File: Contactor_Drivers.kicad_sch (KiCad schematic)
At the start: 37 parts, among them Con1 LED, Con2 LED, Con3 LED, Con4 LED, J4 Conn_01x05, J5 Conn_01x04, J6 Conn_01x04, J7 Conn_01x04, J8 Conn_01x04, Q4 IRLML0030, Q5 IRLML0030, Q6 IRLML0030, Q7 IRLML0030

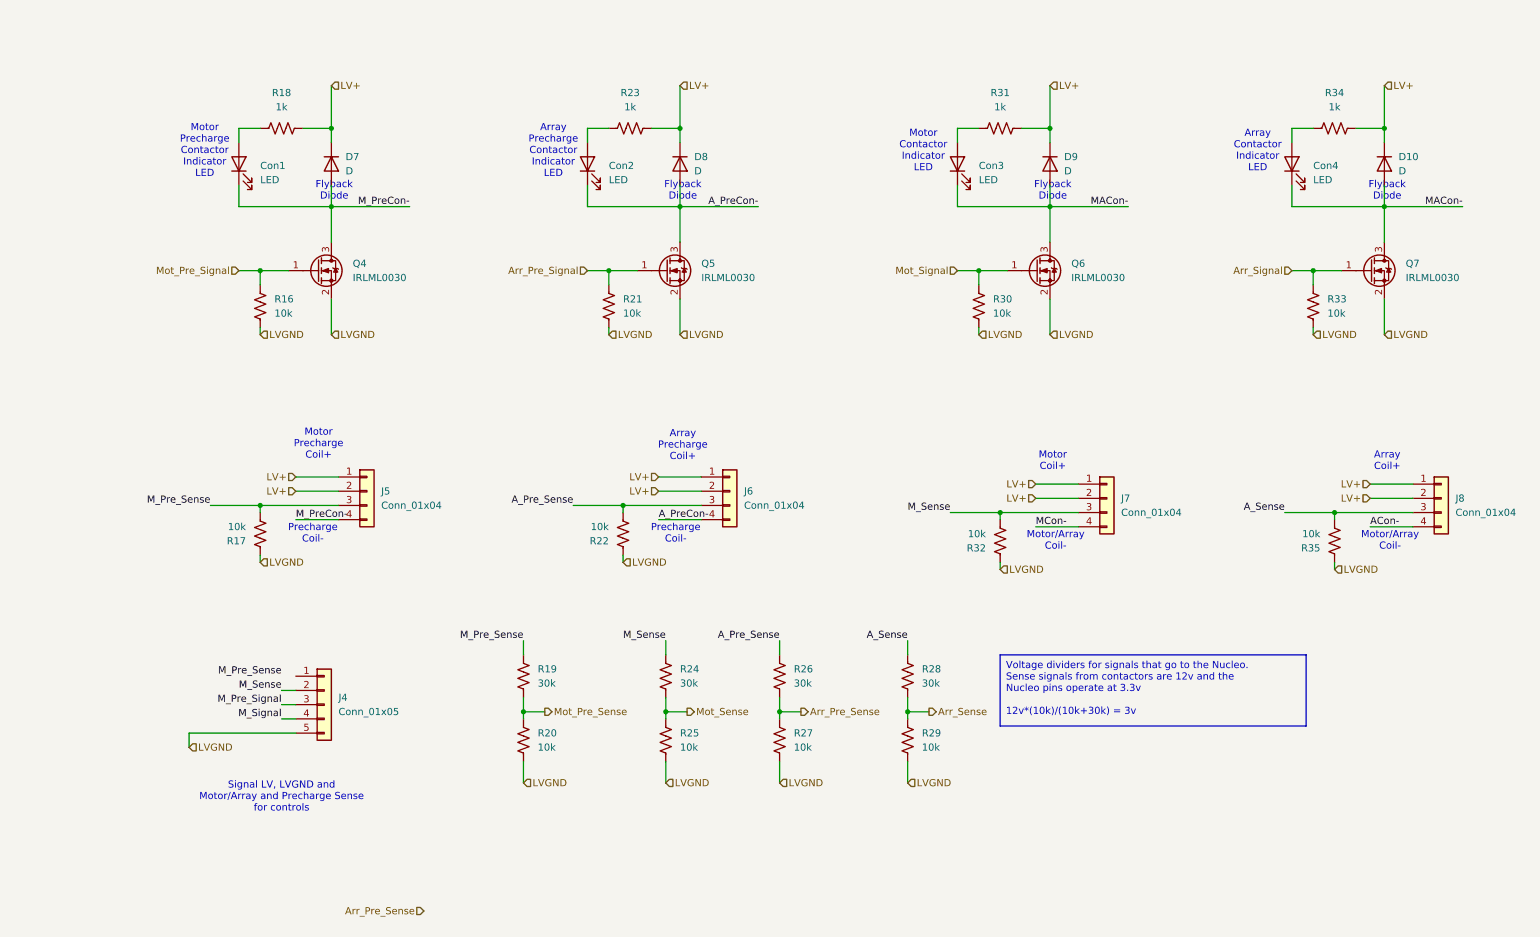
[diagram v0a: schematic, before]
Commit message: fixed some ERC errors, incorrect connectors
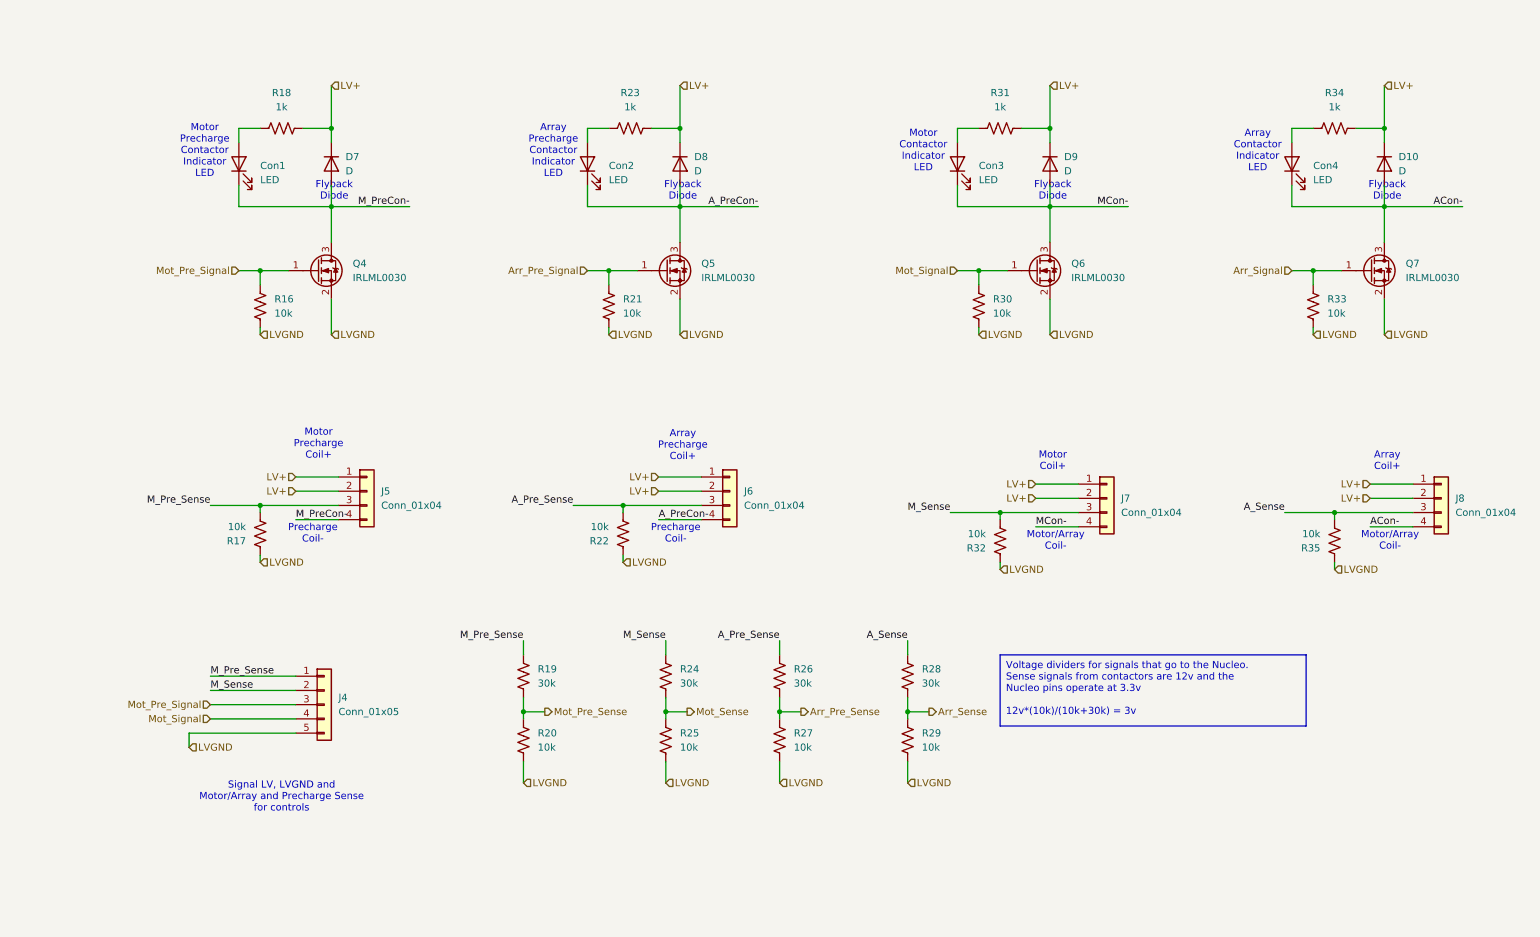
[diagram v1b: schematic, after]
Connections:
- net M_Pre_Signal is gone; now on net Mot_Pre_Signal: J4.3 (Pin_3)
- net M_Signal is gone; now on net Mot_Signal: J4.4 (Pin_4)
- net ACon-: now also Con4.1 (K), D10.2 (A), Q7.3 (D)
- net MCon-: now also Con3.1 (K), D9.2 (A), Q6.3 (D)
- net M_Pre_Sense: now also J4.1 (Pin_1)
- removed net MACon-: Con3.1 (K), Con4.1 (K), D10.2 (A), D9.2 (A), Q6.3 (D), Q7.3 (D)
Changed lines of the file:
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@@
 	(wire
 		(pts
-			(xy 58.42 148.59) (xy 60.96 148.59)
+			(xy 45.72 148.59) (xy 60.96 148.59)
 		)
 		(stroke
@@
 	(wire
 		(pts
+			(xy 45.72 140.97) (xy 60.96 140.97)
+		)
+		(stroke
+			(width 0)
+			(type default)
+		)
+	)
+	(wire
+		(pts
 			(xy 54.61 110.49) (xy 54.61 111.76)
 		)
@@
 	(wire
 		(pts
-			(xy 58.42 146.05) (xy 60.96 146.05)
+			(xy 45.72 146.05) (xy 60.96 146.05)
 		)
 		(stroke
@@
 	(wire
 		(pts
-			(xy 58.42 143.51) (xy 60.96 143.51)
+			(xy 45.72 143.51) (xy 60.96 143.51)
 		)
 		(stroke
@@
 		)
 	)
-	(label "MACon-"
+	(label "ACon-"
 		(at 269.24 57.15 180)
-		(fields_autoplaced yes)
-		(effects
-			(font
-				(size 1.27 1.27)
-			)
-			(justify right bottom)
-		)
-	)
-	(label "M_Pre_Signal"
-		(at 58.42 146.05 180)
 		(fields_autoplaced yes)
 		(effects
@@
 		)
 	)
-	(label "M_Signal"
-		(at 58.42 148.59 180)
-		(fields_autoplaced yes)
-		(effects
-			(font
-				(size 1.27 1.27)
-			)
-			(justify right bottom)
-		)
-	)
 	(label "ACon-"
 		(at 252.73 114.3 0)
@@
 		)
 	)
-	(label "MACon-"
+	(label "MCon-"
 		(at 209.55 57.15 180)
 		(fields_autoplaced yes)
@@
 	)
 	(label "M_Pre_Sense"
-		(at 58.42 140.97 180)
-		(fields_autoplaced yes)
-		(effects
-			(font
-				(size 1.27 1.27)
-			)
-			(justify right bottom)
+		(at 45.72 140.97 0)
+		(fields_autoplaced yes)
+		(effects
+			(font
+				(size 1.27 1.27)
+			)
+			(justify left bottom)
 		)
 	)
@@
 	)
 	(label "M_Sense"
-		(at 58.42 143.51 180)
-		(fields_autoplaced yes)
-		(effects
-			(font
-				(size 1.27 1.27)
-			)
-			(justify right bottom)
+		(at 45.72 143.51 0)
+		(fields_autoplaced yes)
+		(effects
+			(font
+				(size 1.27 1.27)
+			)
+			(justify left bottom)
 		)
 	)
@@
 		)
 	)
+	(hierarchical_label "Mot_Pre_Signal"
+		(shape input)
+		(at 45.72 146.05 180)
+		(fields_autoplaced yes)
+		(effects
+			(font
+				(size 1.27 1.27)
+			)
+			(justify right)
+		)
+	)
 	(hierarchical_label "Arr_Pre_Signal"
 		(shape input)
@@
 			)
 			(justify left)
-		)
-	)
-	(hierarchical_label "Arr_Pre_Sense"
-		(shape input)
-		(at 83.82 182.88 180)
-		(fields_autoplaced yes)
-		(effects
-			(font
-				(size 1.27 1.27)
-			)
-			(justify right)
 		)
 	)
@@
 		)
 	)
+	(hierarchical_label "Mot_Signal"
+		(shape input)
+		(at 45.72 148.59 180)
+		(fields_autoplaced yes)
+		(effects
+			(font
+				(size 1.27 1.27)
+			)
+			(justify right)
+		)
+	)

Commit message: started on HV layout
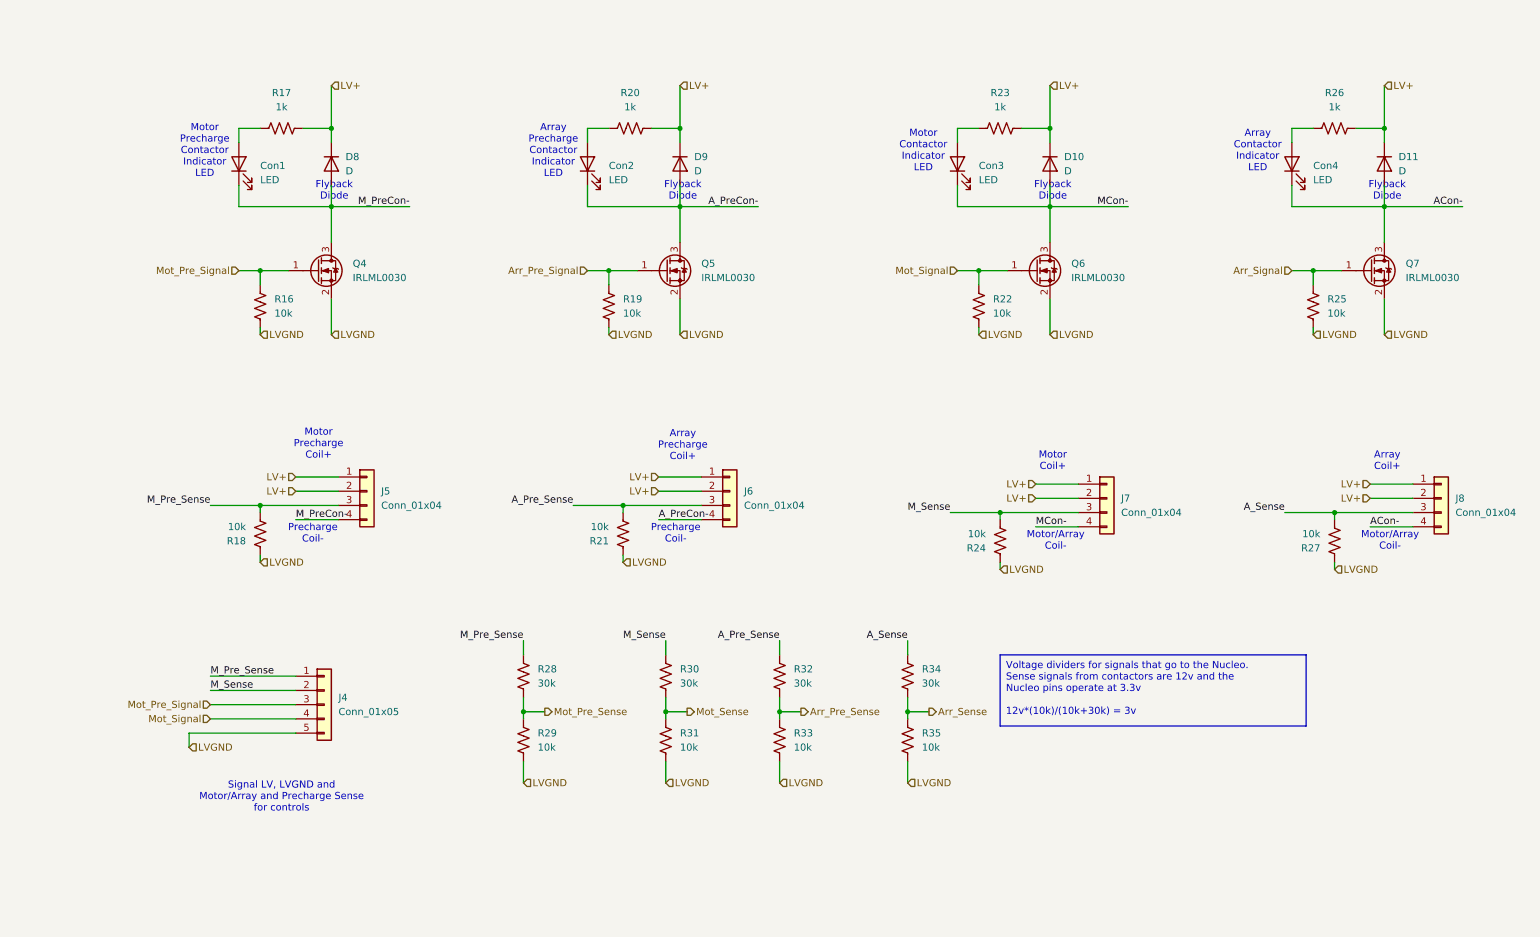
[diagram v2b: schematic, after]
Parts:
- renumbered D9 to D10, D10 to D11, D7 to D8, D8 to D9, R18 to R17, R17 to R18, R21 to R19, R23 to R20, R22 to R21, R30 to R22, R31 to R23, R32 to R24, R33 to R25, R34 to R26, R35 to R27, R19 to R28, R20 to R29, R24 to R30, R25 to R31, R26 to R32, R27 to R33, R28 to R34, R29 to R35
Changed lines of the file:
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@@
 		(on_board yes)
 		(dnp no)
-		(property "Reference" "R22"
+		(property "Reference" "R21"
 			(at 116.84 116.8401 0)
 			(effects
@@
 			(project "ActivePrecharge"
 				(path "/b9847a31-2b3b-47ca-9561-fab506416f6d/c0036b4f-8078-47a1-85ab-72dbdcf28d35"
-					(reference "R22")
+					(reference "R21")
 					(unit 1)
 				)
@@
 		(dnp no)
 		(fields_autoplaced yes)
-		(property "Reference" "R19"
+		(property "Reference" "R28"
 			(at 104.14 139.6999 0)
 			(effects
@@
 			(project "ActivePrecharge"
 				(path "/b9847a31-2b3b-47ca-9561-fab506416f6d/c0036b4f-8078-47a1-85ab-72dbdcf28d35"
-					(reference "R19")
+					(reference "R28")
 					(unit 1)
 				)
@@
 		(on_board yes)
 		(dnp no)
-		(property "Reference" "R30"
+		(property "Reference" "R22"
 			(at 185.42 73.6599 0)
 			(effects
@@
 			(project "ActivePrecharge"
 				(path "/b9847a31-2b3b-47ca-9561-fab506416f6d/c0036b4f-8078-47a1-85ab-72dbdcf28d35"
-					(reference "R30")
+					(reference "R22")
 					(unit 1)
 				)
@@
 		(dnp no)
 		(fields_autoplaced yes)
-		(property "Reference" "D10"
+		(property "Reference" "D11"
 			(at 257.81 48.2599 90)
 			(effects
@@
 			(project "ActivePrecharge"
 				(path "/b9847a31-2b3b-47ca-9561-fab506416f6d/c0036b4f-8078-47a1-85ab-72dbdcf28d35"
-					(reference "D10")
+					(reference "D11")
 					(unit 1)
 				)
@@
 		(dnp no)
 		(fields_autoplaced yes)
-		(property "Reference" "R18"
+		(property "Reference" "R17"
 			(at 58.42 36.83 90)
 			(effects
@@
 			(project "ActivePrecharge"
 				(path "/b9847a31-2b3b-47ca-9561-fab506416f6d/c0036b4f-8078-47a1-85ab-72dbdcf28d35"
-					(reference "R18")
+					(reference "R17")
 					(unit 1)
 				)
@@
 		(dnp no)
 		(fields_autoplaced yes)
-		(property "Reference" "R20"
+		(property "Reference" "R29"
 			(at 104.14 151.1299 0)
 			(effects
@@
 			(project "ActivePrecharge"
 				(path "/b9847a31-2b3b-47ca-9561-fab506416f6d/c0036b4f-8078-47a1-85ab-72dbdcf28d35"
-					(reference "R20")
+					(reference "R29")
 					(unit 1)
 				)
@@
 		(dnp no)
 		(fields_autoplaced yes)
-		(property "Reference" "D8"
+		(property "Reference" "D9"
 			(at 132.08 48.2599 90)
 			(effects
@@
 			(project "ActivePrecharge"
 				(path "/b9847a31-2b3b-47ca-9561-fab506416f6d/c0036b4f-8078-47a1-85ab-72dbdcf28d35"
-					(reference "D8")
+					(reference "D9")
 					(unit 1)
 				)
@@
 		(dnp no)
 		(fields_autoplaced yes)
-		(property "Reference" "R28"
+		(property "Reference" "R34"
 			(at 172.72 139.6999 0)
 			(effects
@@
 			(project "ActivePrecharge"
 				(path "/b9847a31-2b3b-47ca-9561-fab506416f6d/c0036b4f-8078-47a1-85ab-72dbdcf28d35"
-					(reference "R28")
+					(reference "R34")
 					(unit 1)
 				)
@@
 		(dnp no)
 		(fields_autoplaced yes)
-		(property "Reference" "R25"
+		(property "Reference" "R31"
 			(at 129.54 151.1299 0)
 			(effects
@@
 			(project "ActivePrecharge"
 				(path "/b9847a31-2b3b-47ca-9561-fab506416f6d/c0036b4f-8078-47a1-85ab-72dbdcf28d35"
-					(reference "R25")
+					(reference "R31")
 					(unit 1)
 				)
@@
 		(dnp no)
 		(fields_autoplaced yes)
-		(property "Reference" "D9"
+		(property "Reference" "D10"
 			(at 198.12 48.2599 90)
 			(effects
@@
 			(project "ActivePrecharge"
 				(path "/b9847a31-2b3b-47ca-9561-fab506416f6d/c0036b4f-8078-47a1-85ab-72dbdcf28d35"
-					(reference "D9")
+					(reference "D10")
 					(unit 1)
 				)
@@
 		(dnp no)
 		(fields_autoplaced yes)
-		(property "Reference" "R24"
+		(property "Reference" "R30"
 			(at 129.54 139.6999 0)
 			(effects
@@
 			(project "ActivePrecharge"
 				(path "/b9847a31-2b3b-47ca-9561-fab506416f6d/c0036b4f-8078-47a1-85ab-72dbdcf28d35"
-					(reference "R24")
+					(reference "R30")
 					(unit 1)
 				)
@@
 		(on_board yes)
 		(dnp no)
-		(property "Reference" "R33"
+		(property "Reference" "R25"
 			(at 245.11 73.6599 0)
 			(effects
@@
 			(project "ActivePrecharge"
 				(path "/b9847a31-2b3b-47ca-9561-fab506416f6d/c0036b4f-8078-47a1-85ab-72dbdcf28d35"
-					(reference "R33")
+					(reference "R25")
 					(unit 1)
 				)
@@
 		(dnp no)
 		(fields_autoplaced yes)
-		(property "Reference" "R29"
+		(property "Reference" "R35"
 			(at 172.72 151.1299 0)
 			(effects
@@
 			(project "ActivePrecharge"
 				(path "/b9847a31-2b3b-47ca-9561-fab506416f6d/c0036b4f-8078-47a1-85ab-72dbdcf28d35"
-					(reference "R29")
+					(reference "R35")
 					(unit 1)
 				)
@@
 		(on_board yes)
 		(dnp no)
-		(property "Reference" "R21"
+		(property "Reference" "R19"
 			(at 119.38 73.6599 0)
 			(effects
@@
 			(project "ActivePrecharge"
 				(path "/b9847a31-2b3b-47ca-9561-fab506416f6d/c0036b4f-8078-47a1-85ab-72dbdcf28d35"
-					(reference "R21")
+					(reference "R19")
 					(unit 1)
 				)
@@
 		(on_board yes)
 		(dnp no)
-		(property "Reference" "R17"
+		(property "Reference" "R18"
 			(at 52.07 116.8401 0)
 			(effects
@@
 			(project "ActivePrecharge"
 				(path "/b9847a31-2b3b-47ca-9561-fab506416f6d/c0036b4f-8078-47a1-85ab-72dbdcf28d35"
-					(reference "R17")
+					(reference "R18")
 					(unit 1)
 				)
@@
 		(dnp no)
 		(fields_autoplaced yes)
-		(property "Reference" "R31"
+		(property "Reference" "R23"
 			(at 186.69 36.83 90)
 			(effects
@@
 			(project "ActivePrecharge"
 				(path "/b9847a31-2b3b-47ca-9561-fab506416f6d/c0036b4f-8078-47a1-85ab-72dbdcf28d35"
-					(reference "R31")
+					(reference "R23")
 					(unit 1)
 				)
@@
 		(dnp no)
 		(fields_autoplaced yes)
-		(property "Reference" "R26"
+		(property "Reference" "R32"
 			(at 149.86 139.6999 0)
 			(effects
@@
 			(project "ActivePrecharge"
 				(path "/b9847a31-2b3b-47ca-9561-fab506416f6d/c0036b4f-8078-47a1-85ab-72dbdcf28d35"
-					(reference "R26")
+					(reference "R32")
 					(unit 1)
 				)
@@
 		(dnp no)
 		(fields_autoplaced yes)
-		(property "Reference" "R23"
+		(property "Reference" "R20"
 			(at 120.65 36.83 90)
 			(effects
@@
 			(project "ActivePrecharge"
 				(path "/b9847a31-2b3b-47ca-9561-fab506416f6d/c0036b4f-8078-47a1-85ab-72dbdcf28d35"
-					(reference "R23")
+					(reference "R20")
 					(unit 1)
 				)
@@
 		(dnp no)
 		(fields_autoplaced yes)
-		(property "Reference" "R27"
+		(property "Reference" "R33"
 			(at 149.86 151.1299 0)
 			(effects
@@
 			(project "ActivePrecharge"
 				(path "/b9847a31-2b3b-47ca-9561-fab506416f6d/c0036b4f-8078-47a1-85ab-72dbdcf28d35"
-					(reference "R27")
+					(reference "R33")
 					(unit 1)
 				)
@@
 		(dnp no)
 		(fields_autoplaced yes)
-		(property "Reference" "R34"
+		(property "Reference" "R26"
 			(at 246.38 36.83 90)
 			(effects
@@
 			(project "ActivePrecharge"
 				(path "/b9847a31-2b3b-47ca-9561-fab506416f6d/c0036b4f-8078-47a1-85ab-72dbdcf28d35"
-					(reference "R34")
+					(reference "R26")
 					(unit 1)
 				)
@@
 		(dnp no)
 		(fields_autoplaced yes)
-		(property "Reference" "D7"
+		(property "Reference" "D8"
 			(at 69.85 48.2599 90)
 			(effects
@@
 			(project "ActivePrecharge"
 				(path "/b9847a31-2b3b-47ca-9561-fab506416f6d/c0036b4f-8078-47a1-85ab-72dbdcf28d35"
-					(reference "D7")
+					(reference "D8")
 					(unit 1)
 				)
@@
 		(on_board yes)
 		(dnp no)
-		(property "Reference" "R32"
+		(property "Reference" "R24"
 			(at 184.15 118.1101 0)
 			(effects
@@
 			(project "ActivePrecharge"
 				(path "/b9847a31-2b3b-47ca-9561-fab506416f6d/c0036b4f-8078-47a1-85ab-72dbdcf28d35"
-					(reference "R32")
+					(reference "R24")
 					(unit 1)
 				)
@@
 		(on_board yes)
 		(dnp no)
-		(property "Reference" "R35"
+		(property "Reference" "R27"
 			(at 243.84 118.1101 0)
 			(effects
@@
 			(project "ActivePrecharge"
 				(path "/b9847a31-2b3b-47ca-9561-fab506416f6d/c0036b4f-8078-47a1-85ab-72dbdcf28d35"
-					(reference "R35")
-					(unit 1)
-				)
+					(reference "R27")
+					(unit 1)
+				)
